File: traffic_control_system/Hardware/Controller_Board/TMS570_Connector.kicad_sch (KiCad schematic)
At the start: 3 parts, among them J1 Conn_02x33_Odd_Even, J2 Conn_02x33_Odd_Even, J3 Conn_02x40_Odd_Even

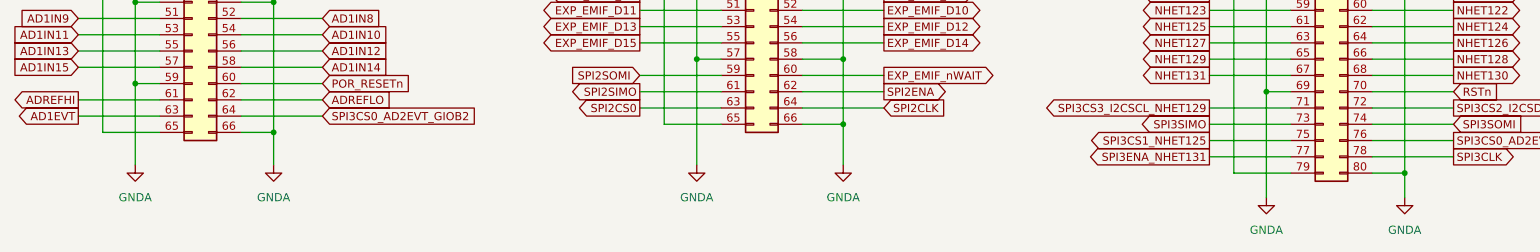
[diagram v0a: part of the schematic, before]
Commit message: issue : 회로 오타 수정[ISSUE-5]
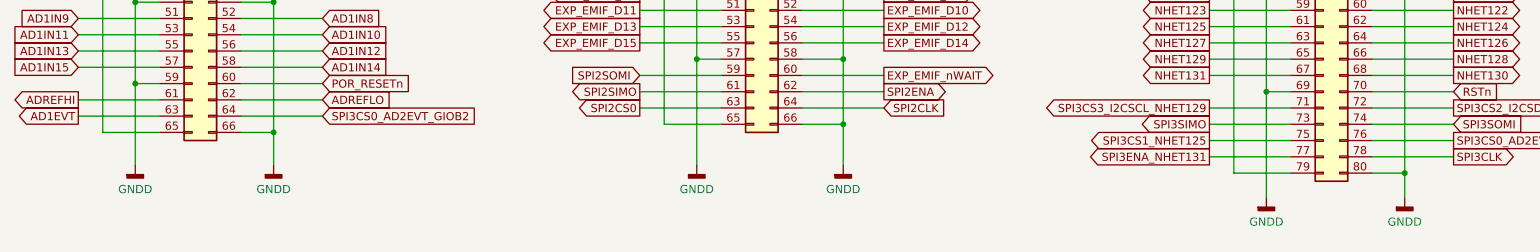
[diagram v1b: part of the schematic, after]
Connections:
- net GNDA renamed GNDD
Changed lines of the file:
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@@
   (title_block
     (title "TMS570_Connector")
-    (date "2022-06-21")
-    (rev "rev00")
+    (date "2022-07-01")
+    (rev "rev01")
   )
   (junction (at 154.94 91.44) (diameter 0) (color 0 0 0 0)
@@
     (pin "9")
   )
+  (symbol (lib_id "power:GNDD") (at 44.45 130.81 0) (unit 1)
+    (in_bom yes) (on_board yes)
+    (property "Reference" "#PWR?" (id 0) (at 44.45 137.16 0)
+      (effects (font (size 1.27 1.27)) hide)
+    )
+    (property "Value" "GNDD" (id 1) (at 44.45 134.62 0))
+    (property "Footprint" "" (id 2) (at 44.45 130.81 0)
+      (effects (font (size 1.27 1.27)) hide)
+    )
+    (property "Datasheet" "" (id 3) (at 44.45 130.81 0)
+      (effects (font (size 1.27 1.27)) hide)
+    )
+    (pin "1")
+  )
   (symbol (lib_name "+12VA_2") (lib_id "power:+12VA") (at 215.9 30.48 0) (unit 1)
     (in_bom yes) (on_board yes) (fields_autoplaced)
@@
     (pin "1")
   )
-  (symbol (lib_id "power:GNDA") (at 220.98 135.89 0) (unit 1)
-    (in_bom yes) (on_board yes) (fields_autoplaced)
-    (property "Reference" "#PWR08" (id 0) (at 220.98 142.24 0)
-      (effects (font (size 1.27 1.27)) hide)
-    )
-    (property "Value" "GNDA" (id 1) (at 220.98 140.97 0))
+  (symbol (lib_id "power:GNDD") (at 220.98 135.89 0) (unit 1)
+    (in_bom yes) (on_board yes)
+    (property "Reference" "#PWR?" (id 0) (at 220.98 142.24 0)
+      (effects (font (size 1.27 1.27)) hide)
+    )
+    (property "Value" "GNDD" (id 1) (at 220.98 139.7 0))
     (property "Footprint" "" (id 2) (at 220.98 135.89 0)
       (effects (font (size 1.27 1.27)) hide)
@@
     (pin "1")
   )
-  (symbol (lib_id "power:GNDA") (at 66.04 130.81 0) (unit 1)
-    (in_bom yes) (on_board yes) (fields_autoplaced)
-    (property "Reference" "#PWR03" (id 0) (at 66.04 137.16 0)
-      (effects (font (size 1.27 1.27)) hide)
-    )
-    (property "Value" "GNDA" (id 1) (at 66.04 135.89 0))
-    (property "Footprint" "" (id 2) (at 66.04 130.81 0)
-      (effects (font (size 1.27 1.27)) hide)
-    )
-    (property "Datasheet" "" (id 3) (at 66.04 130.81 0)
+  (symbol (lib_id "power:GNDD") (at 242.57 135.89 0) (unit 1)
+    (in_bom yes) (on_board yes)
+    (property "Reference" "#PWR?" (id 0) (at 242.57 142.24 0)
+      (effects (font (size 1.27 1.27)) hide)
+    )
+    (property "Value" "GNDD" (id 1) (at 242.57 139.7 0))
+    (property "Footprint" "" (id 2) (at 242.57 135.89 0)
+      (effects (font (size 1.27 1.27)) hide)
+    )
+    (property "Datasheet" "" (id 3) (at 242.57 135.89 0)
       (effects (font (size 1.27 1.27)) hide)
     )
@@
     (pin "1")
   )
-  (symbol (lib_id "power:GNDA") (at 44.45 130.81 0) (unit 1)
-    (in_bom yes) (on_board yes) (fields_autoplaced)
-    (property "Reference" "#PWR02" (id 0) (at 44.45 137.16 0)
-      (effects (font (size 1.27 1.27)) hide)
-    )
-    (property "Value" "GNDA" (id 1) (at 44.45 135.89 0))
-    (property "Footprint" "" (id 2) (at 44.45 130.81 0)
-      (effects (font (size 1.27 1.27)) hide)
-    )
-    (property "Datasheet" "" (id 3) (at 44.45 130.81 0)
+  (symbol (lib_id "power:GNDD") (at 66.04 130.81 0) (unit 1)
+    (in_bom yes) (on_board yes)
+    (property "Reference" "#PWR?" (id 0) (at 66.04 137.16 0)
+      (effects (font (size 1.27 1.27)) hide)
+    )
+    (property "Value" "GNDD" (id 1) (at 66.04 134.62 0))
+    (property "Footprint" "" (id 2) (at 66.04 130.81 0)
+      (effects (font (size 1.27 1.27)) hide)
+    )
+    (property "Datasheet" "" (id 3) (at 66.04 130.81 0)
       (effects (font (size 1.27 1.27)) hide)
     )
     (pin "1")
   )
-  (symbol (lib_id "power:GNDA") (at 242.57 135.89 0) (unit 1)
-    (in_bom yes) (on_board yes) (fields_autoplaced)
-    (property "Reference" "#PWR09" (id 0) (at 242.57 142.24 0)
-      (effects (font (size 1.27 1.27)) hide)
-    )
-    (property "Value" "GNDA" (id 1) (at 242.57 140.97 0))
-    (property "Footprint" "" (id 2) (at 242.57 135.89 0)
-      (effects (font (size 1.27 1.27)) hide)
-    )
-    (property "Datasheet" "" (id 3) (at 242.57 135.89 0)
+  (symbol (lib_id "power:GNDD") (at 132.08 130.81 0) (unit 1)
+    (in_bom yes) (on_board yes)
+    (property "Reference" "#PWR?" (id 0) (at 132.08 137.16 0)
+      (effects (font (size 1.27 1.27)) hide)
+    )
+    (property "Value" "GNDD" (id 1) (at 132.08 134.62 0))
+    (property "Footprint" "" (id 2) (at 132.08 130.81 0)
+      (effects (font (size 1.27 1.27)) hide)
+    )
+    (property "Datasheet" "" (id 3) (at 132.08 130.81 0)
       (effects (font (size 1.27 1.27)) hide)
     )
@@
     (pin "9")
   )
-  (symbol (lib_id "power:GNDA") (at 154.94 130.81 0) (unit 1)
-    (in_bom yes) (on_board yes) (fields_autoplaced)
-    (property "Reference" "#PWR06" (id 0) (at 154.94 137.16 0)
-      (effects (font (size 1.27 1.27)) hide)
-    )
-    (property "Value" "GNDA" (id 1) (at 154.94 135.89 0))
-    (property "Footprint" "" (id 2) (at 154.94 130.81 0)
-      (effects (font (size 1.27 1.27)) hide)
-    )
-    (property "Datasheet" "" (id 3) (at 154.94 130.81 0)
-      (effects (font (size 1.27 1.27)) hide)
-    )
-    (pin "1")
-  )
-  (symbol (lib_id "power:GNDA") (at 132.08 130.81 0) (unit 1)
-    (in_bom yes) (on_board yes) (fields_autoplaced)
-    (property "Reference" "#PWR05" (id 0) (at 132.08 137.16 0)
-      (effects (font (size 1.27 1.27)) hide)
-    )
-    (property "Value" "GNDA" (id 1) (at 132.08 135.89 0))
-    (property "Footprint" "" (id 2) (at 132.08 130.81 0)
-      (effects (font (size 1.27 1.27)) hide)
-    )
-    (property "Datasheet" "" (id 3) (at 132.08 130.81 0)
-      (effects (font (size 1.27 1.27)) hide)
-    )
-    (pin "1")
-  )
   (symbol (lib_name "+12VA_1") (lib_id "power:+12VA") (at 39.37 41.91 0) (unit 1)
     (in_bom yes) (on_board yes) (fields_autoplaced)
@@
       (effects (font (size 1.27 1.27)) hide)
     )
+    (pin "1")
+  )
+  (symbol (lib_id "power:GNDD") (at 154.94 130.81 0) (unit 1)
+    (in_bom yes) (on_board yes)
+    (property "Reference" "#PWR?" (id 0) (at 154.94 137.16 0)
+      (effects (font (size 1.27 1.27)) hide)
+    )
+    (property "Value" "GNDD" (id 1) (at 154.94 134.62 0))
+    (property "Footprint" "" (id 2) (at 154.94 130.81 0)
+      (effects (font (size 1.27 1.27)) hide)
+    )
+    (property "Datasheet" "" (id 3) (at 154.94 130.81 0)
+      (effects (font (size 1.27 1.27)) hide)
+    )
